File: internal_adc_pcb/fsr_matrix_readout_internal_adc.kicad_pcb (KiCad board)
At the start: 2 copper layers, 50 x 65 mm, 97 parts, among them J1 Conn_01x22, J2 Conn_01x22, U1 RS2323XUTQK10, U10 TLV9061xDBV, U11 SN74AHC138RGYR, U12 SN74AHC138RGYR, U13 SN74LVC1G14DCKR_C19829630, U14 TLV9064, U15 TLV9064, U16 TLV9064, U17 TLV9064, U2 RS2323XUTQK10, U3 RS2323XUTQK10, U4 RS2323XUTQK10, U5 RS2323XUTQK10, U6 RS2323XUTQK10, U7 RS2323XUTQK10, U8 RS2323XUTQK10, U9 TPS7A2033PDBVR

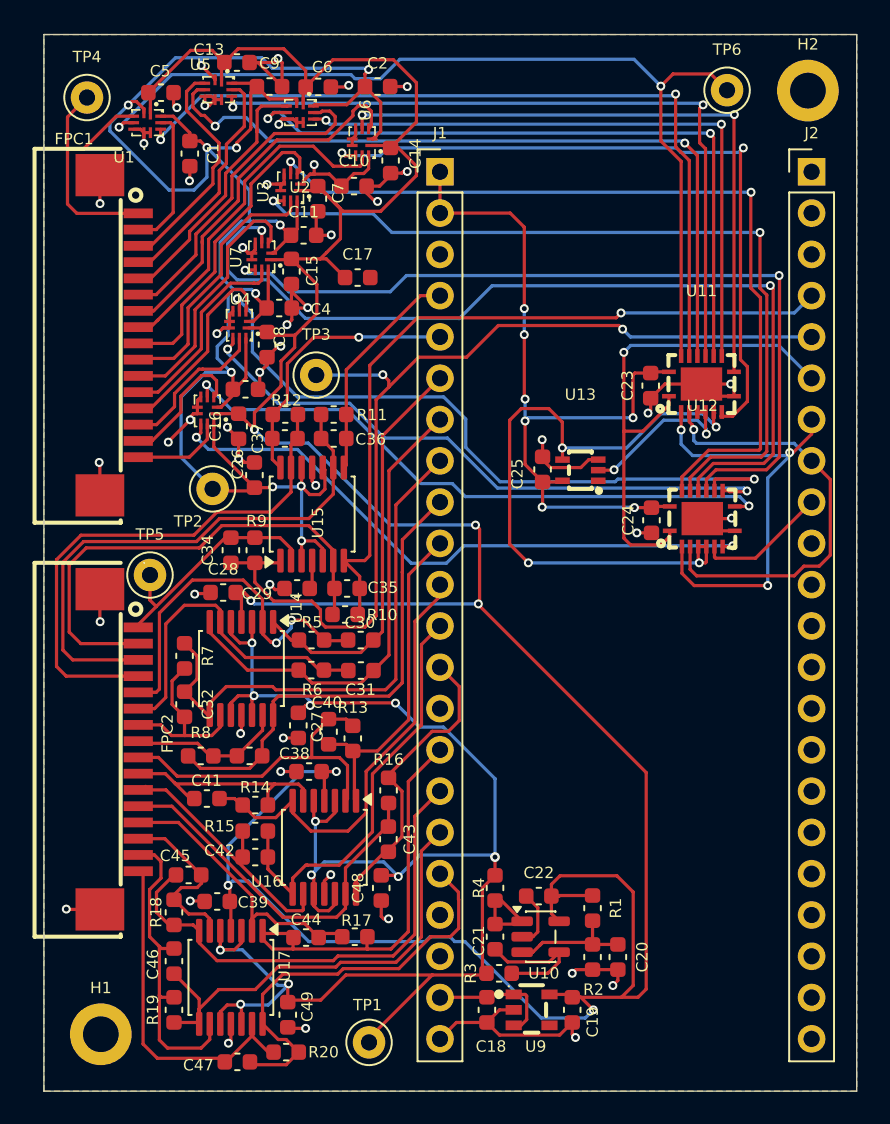
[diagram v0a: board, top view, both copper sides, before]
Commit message: change ESP connector from pin to socket
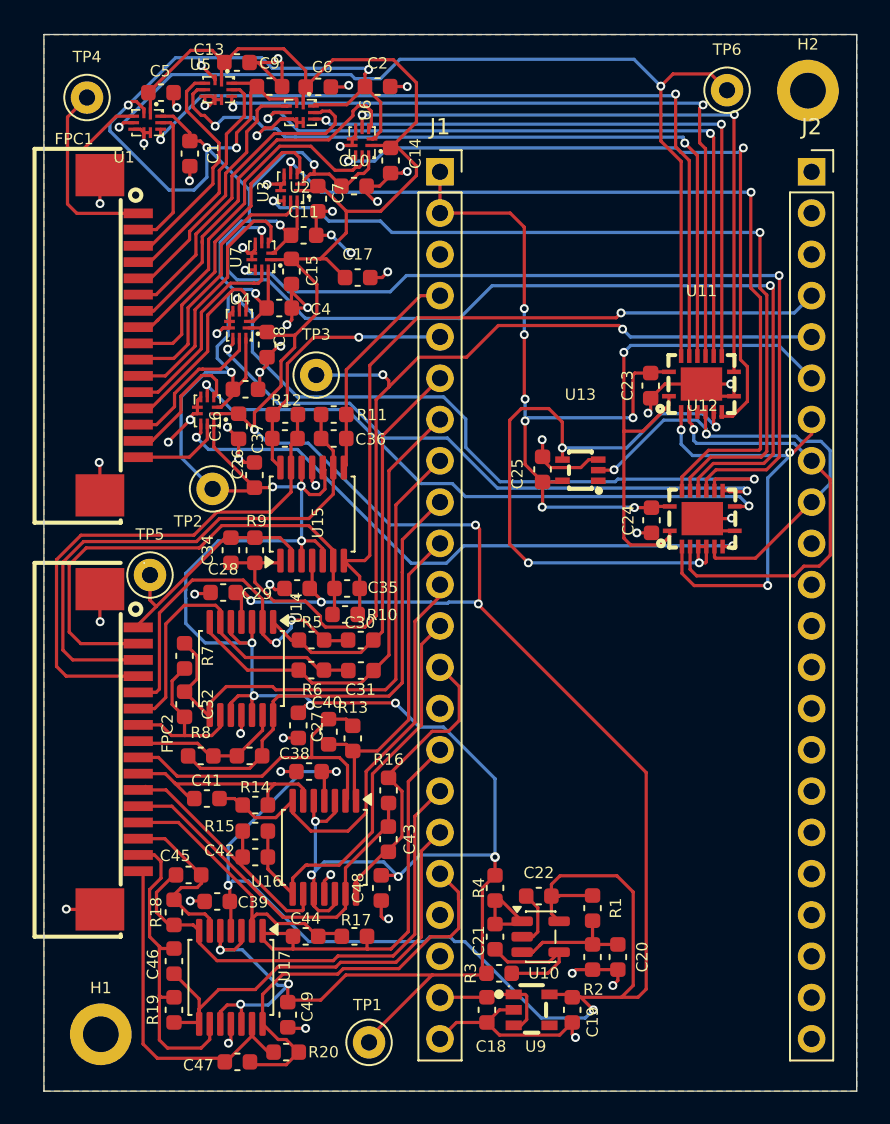
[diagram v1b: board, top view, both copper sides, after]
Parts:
- J1, J2: footprint Connector_PinHeader_2.54mm:PinHeader_1x22_P2.54mm_Vertical -> Connector_PinSocket_2.54mm:PinSocket_1x22_P2.54mm_Vertical
- moved C44 0.08 mm to (109.1, 81.5)
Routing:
- net /16x Frontend Analog Switch/VG: track 231.6 -> 252.5 mm
- net /4_to_16 Decoder/A3: track 18.4 -> 30.1 mm
- net GND: track 105.0 -> 111.2 mm, vias 45 -> 49
- net +3V3: track 209.4 -> 208.7 mm, vias 7 -> 8
